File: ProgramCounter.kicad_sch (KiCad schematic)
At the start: 11 parts, among them U601 74LS161, U602 74LS161, U603 74HC245, U604 74HC245, U605 74HC245

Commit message: Working
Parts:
- removed C605, C606: C, symbol Device:C
- removed U605: 74HC245, symbol 74xx:74HC245
- added C805: C, symbol Device:C
- added U805: 74LS32, symbol 74xx:74LS32
- renumbered C601 to C801, C602 to C802, C603 to C803, C604 to C804, U603 to U801, U604 to U802, U601 to U803, U602 to U804
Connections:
- net Bus_{0} is gone; now on net PC_{0}: U801.2 (A0), U802.2 (A0), U803.14 (Q0)
- net Bus_{1} is gone; now on net PC_{1}: U801.3 (A1), U802.3 (A1), U803.13 (Q1)
- net Bus_{2} is gone; now on net PC_{2}: U801.4 (A2), U802.4 (A2), U803.12 (Q2)
- net Bus_{3} is gone; now on net PC_{3}: U801.5 (A3), U802.5 (A3), U803.11 (Q3)
- net Bus_{4} is gone; now on net PC_{4}: U801.6 (A4), U802.6 (A4), U804.14 (Q0)
- net Bus_{5} is gone; now on net PC_{5}: U801.7 (A5), U802.7 (A5), U804.13 (Q1)
- net Bus_{6} is gone; now on net PC_{6}: U801.8 (A6), U802.8 (A6), U804.12 (Q2)
- net Bus_{7} is gone; now on net PC_{7}: U801.9 (A7), U802.9 (A7), U804.11 (Q3)
- net +5V: now also C805.1, U805.14 (VCC)
- net GND: now also C805.2, U805.10, U805.12, U805.13, U805.7 (GND), U805.9
- net ~{LoadHigh}: now also U805.4; no longer U804.9 (~{PE})
- net ~{LoadLow}: now also U805.1; no longer U803.9 (~{PE})
- new net ~{Load}: U805.2, U805.5
- new net ~{PE_High}: U804.9 (~{PE}), U805.6
- new net ~{PE_Low}: U803.9 (~{PE}), U805.3
- no-connect marks 1 -> 3
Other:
- moved on the sheet: C801, C802, C803, C804

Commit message: Reorganize Registerfile
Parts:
- removed C805: C, symbol Device:C
- removed U805: 74LS32, symbol 74xx:74LS32
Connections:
- net ~{PE_High} is gone; now on net ~{LoadHigh}: U804.9 (~{PE})
- net ~{PE_Low} is gone; now on net ~{LoadLow}: U803.9 (~{PE})
- no-connect marks 3 -> 1
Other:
- moved on the sheet: C801, C802, C803, C804

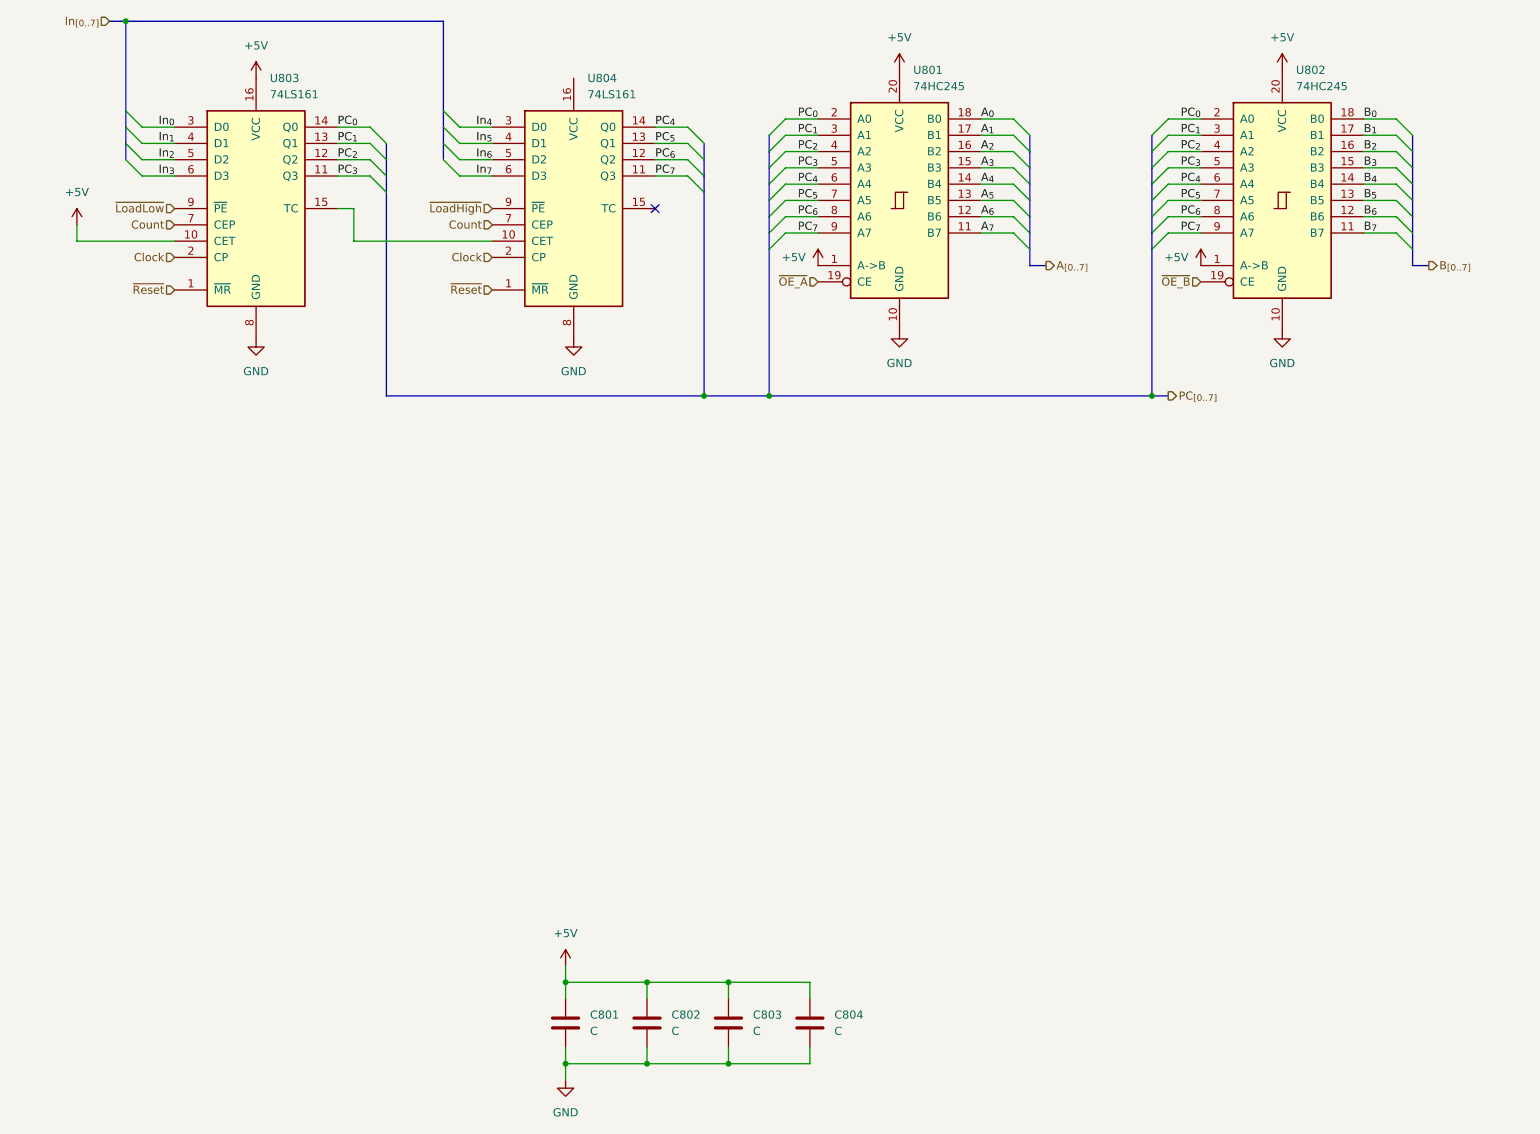
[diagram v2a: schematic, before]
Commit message: More cleanup and preparing signals for control logic
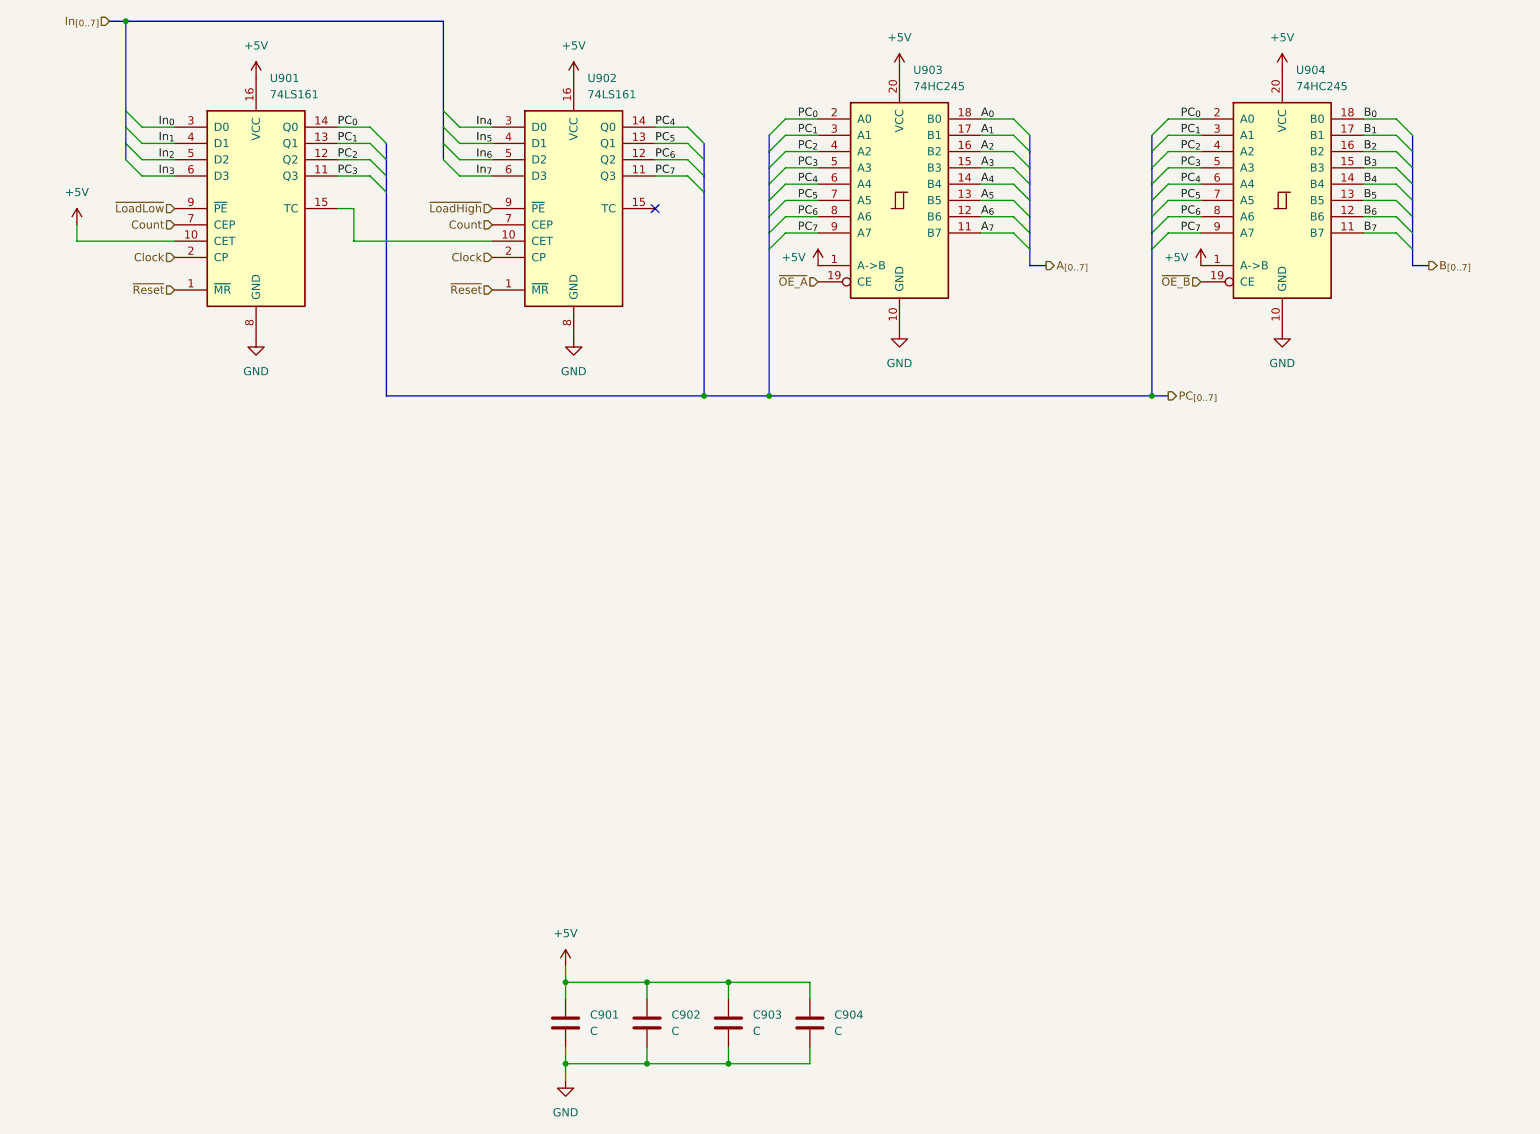
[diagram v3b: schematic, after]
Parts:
- renumbered C801 to C901, C802 to C902, C803 to C903, C804 to C904, U803 to U901, U804 to U902, U801 to U903, U802 to U904
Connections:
- net +5V: now also U902.16 (VCC)
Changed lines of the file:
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@@
 		(dnp no)
 		(fields_autoplaced yes)
-		(property "Reference" "#PWR0804"
+		(property "Reference" "#PWR0901"
 			(at 33.02 62.23 0)
 			(effects
@@
 			(project "BRISC8"
 				(path "/e198223b-f7bd-4b26-ae2e-259db8d07fb6/d081cdcb-1181-4657-9580-dc3ba9a85775/ded358fb-ee52-4096-a32a-0cce52708100/0c7a1bf0-e6ae-42c1-a12c-9c71b98ed1be"
-					(reference "#PWR0804")
+					(reference "#PWR0901")
 					(unit 1)
 				)
@@
 		(on_board yes)
 		(dnp no)
-		(property "Reference" "#PWR0806"
+		(property "Reference" "#PWR0911"
 			(at 208.28 68.58 0)
 			(effects
@@
 			(project "BRISC8"
 				(path "/e198223b-f7bd-4b26-ae2e-259db8d07fb6/d081cdcb-1181-4657-9580-dc3ba9a85775/ded358fb-ee52-4096-a32a-0cce52708100/0c7a1bf0-e6ae-42c1-a12c-9c71b98ed1be"
-					(reference "#PWR0806")
+					(reference "#PWR0911")
 					(unit 1)
 				)
@@
 		(dnp no)
 		(fields_autoplaced yes)
-		(property "Reference" "#PWR0807"
+		(property "Reference" "#PWR0910"
 			(at 161.29 81.28 0)
 			(effects
@@
 			(project "BRISC8"
 				(path "/e198223b-f7bd-4b26-ae2e-259db8d07fb6/d081cdcb-1181-4657-9580-dc3ba9a85775/ded358fb-ee52-4096-a32a-0cce52708100/0c7a1bf0-e6ae-42c1-a12c-9c71b98ed1be"
-					(reference "#PWR0807")
+					(reference "#PWR0910")
 					(unit 1)
 				)
@@
 		(dnp no)
 		(fields_autoplaced yes)
-		(property "Reference" "C801"
+		(property "Reference" "C901"
 			(at 113.03 181.6099 0)
 			(effects
@@
 			(project "BRISC8"
 				(path "/e198223b-f7bd-4b26-ae2e-259db8d07fb6/d081cdcb-1181-4657-9580-dc3ba9a85775/ded358fb-ee52-4096-a32a-0cce52708100/0c7a1bf0-e6ae-42c1-a12c-9c71b98ed1be"
-					(reference "C801")
+					(reference "C901")
 					(unit 1)
 				)
@@
 		(dnp no)
 		(fields_autoplaced yes)
-		(property "Reference" "#PWR0809"
+		(property "Reference" "#PWR0903"
 			(at 60.96 82.55 0)
 			(effects
@@
 			(project "BRISC8"
 				(path "/e198223b-f7bd-4b26-ae2e-259db8d07fb6/d081cdcb-1181-4657-9580-dc3ba9a85775/ded358fb-ee52-4096-a32a-0cce52708100/0c7a1bf0-e6ae-42c1-a12c-9c71b98ed1be"
-					(reference "#PWR0809")
+					(reference "#PWR0903")
 					(unit 1)
 				)
@@
 		(dnp no)
 		(fields_autoplaced yes)
-		(property "Reference" "#PWR0810"
+		(property "Reference" "#PWR0907"
 			(at 110.49 82.55 0)
 			(effects
@@
 			(project "BRISC8"
 				(path "/e198223b-f7bd-4b26-ae2e-259db8d07fb6/d081cdcb-1181-4657-9580-dc3ba9a85775/ded358fb-ee52-4096-a32a-0cce52708100/0c7a1bf0-e6ae-42c1-a12c-9c71b98ed1be"
-					(reference "#PWR0810")
+					(reference "#PWR0907")
 					(unit 1)
 				)
@@
 		(dnp no)
 		(fields_autoplaced yes)
-		(property "Reference" "#PWR0803"
+		(property "Reference" "#PWR0902"
 			(at 60.96 39.37 0)
 			(effects
@@
 			(project "BRISC8"
 				(path "/e198223b-f7bd-4b26-ae2e-259db8d07fb6/d081cdcb-1181-4657-9580-dc3ba9a85775/ded358fb-ee52-4096-a32a-0cce52708100/0c7a1bf0-e6ae-42c1-a12c-9c71b98ed1be"
-					(reference "#PWR0803")
+					(reference "#PWR0902")
 					(unit 1)
 				)
@@
 		(dnp no)
 		(fields_autoplaced yes)
-		(property "Reference" "C802"
+		(property "Reference" "C902"
 			(at 125.73 181.6099 0)
 			(effects
@@
 			(project "BRISC8"
 				(path "/e198223b-f7bd-4b26-ae2e-259db8d07fb6/d081cdcb-1181-4657-9580-dc3ba9a85775/ded358fb-ee52-4096-a32a-0cce52708100/0c7a1bf0-e6ae-42c1-a12c-9c71b98ed1be"
-					(reference "C802")
+					(reference "C902")
 					(unit 1)
 				)
@@
 		(dnp no)
 		(fields_autoplaced yes)
-		(property "Reference" "#PWR0801"
+		(property "Reference" "#PWR0909"
 			(at 161.29 38.1 0)
 			(effects
@@
 			(project "BRISC8"
 				(path "/e198223b-f7bd-4b26-ae2e-259db8d07fb6/d081cdcb-1181-4657-9580-dc3ba9a85775/ded358fb-ee52-4096-a32a-0cce52708100/0c7a1bf0-e6ae-42c1-a12c-9c71b98ed1be"
-					(reference "#PWR0801")
+					(reference "#PWR0909")
 					(unit 1)
 				)
@@
 		(dnp no)
 		(fields_autoplaced yes)
-		(property "Reference" "U801"
+		(property "Reference" "U903"
 			(at 163.4333 34.29 0)
 			(effects
@@
 			(project "BRISC8"
 				(path "/e198223b-f7bd-4b26-ae2e-259db8d07fb6/d081cdcb-1181-4657-9580-dc3ba9a85775/ded358fb-ee52-4096-a32a-0cce52708100/0c7a1bf0-e6ae-42c1-a12c-9c71b98ed1be"
-					(reference "U801")
+					(reference "U903")
 					(unit 1)
 				)
@@
 		(dnp no)
 		(fields_autoplaced yes)
-		(property "Reference" "U803"
+		(property "Reference" "U901"
 			(at 63.1033 35.56 0)
 			(effects
@@
 			(project "BRISC8"
 				(path "/e198223b-f7bd-4b26-ae2e-259db8d07fb6/d081cdcb-1181-4657-9580-dc3ba9a85775/ded358fb-ee52-4096-a32a-0cce52708100/0c7a1bf0-e6ae-42c1-a12c-9c71b98ed1be"
-					(reference "U803")
+					(reference "U901")
 					(unit 1)
 				)
@@
 		(dnp no)
 		(fields_autoplaced yes)
-		(property "Reference" "U804"
+		(property "Reference" "U902"
 			(at 112.6333 35.56 0)
 			(effects
@@
 			(project "BRISC8"
 				(path "/e198223b-f7bd-4b26-ae2e-259db8d07fb6/d081cdcb-1181-4657-9580-dc3ba9a85775/ded358fb-ee52-4096-a32a-0cce52708100/0c7a1bf0-e6ae-42c1-a12c-9c71b98ed1be"
-					(reference "U804")
+					(reference "U902")
 					(unit 1)
 				)
@@
 		(dnp no)
 		(fields_autoplaced yes)
-		(property "Reference" "C804"
+		(property "Reference" "C904"
 			(at 151.13 181.6099 0)
 			(effects
@@
 			(project "BRISC8"
 				(path "/e198223b-f7bd-4b26-ae2e-259db8d07fb6/d081cdcb-1181-4657-9580-dc3ba9a85775/ded358fb-ee52-4096-a32a-0cce52708100/0c7a1bf0-e6ae-42c1-a12c-9c71b98ed1be"
-					(reference "C804")
+					(reference "C904")
 					(unit 1)
 				)
@@
 		(dnp no)
 		(fields_autoplaced yes)
-		(property "Reference" "#PWR0811"
+		(property "Reference" "#PWR0904"
 			(at 109.22 177.8 0)
 			(effects
@@
 			(project "BRISC8"
 				(path "/e198223b-f7bd-4b26-ae2e-259db8d07fb6/d081cdcb-1181-4657-9580-dc3ba9a85775/ded358fb-ee52-4096-a32a-0cce52708100/0c7a1bf0-e6ae-42c1-a12c-9c71b98ed1be"
-					(reference "#PWR0811")
+					(reference "#PWR0904")
 					(unit 1)
 				)
@@
 		(dnp no)
 		(fields_autoplaced yes)
-		(property "Reference" "#PWR0808"
+		(property "Reference" "#PWR0913"
 			(at 220.98 81.28 0)
 			(effects
@@
 			(project "BRISC8"
 				(path "/e198223b-f7bd-4b26-ae2e-259db8d07fb6/d081cdcb-1181-4657-9580-dc3ba9a85775/ded358fb-ee52-4096-a32a-0cce52708100/0c7a1bf0-e6ae-42c1-a12c-9c71b98ed1be"
-					(reference "#PWR0808")
+					(reference "#PWR0913")
 					(unit 1)
 				)
@@
 		(dnp no)
 		(fields_autoplaced yes)
-		(property "Reference" "#PWR0802"
+		(property "Reference" "#PWR0912"
 			(at 220.98 38.1 0)
 			(effects
@@
 			(project "BRISC8"
 				(path "/e198223b-f7bd-4b26-ae2e-259db8d07fb6/d081cdcb-1181-4657-9580-dc3ba9a85775/ded358fb-ee52-4096-a32a-0cce52708100/0c7a1bf0-e6ae-42c1-a12c-9c71b98ed1be"
-					(reference "#PWR0802")
+					(reference "#PWR0912")
 					(unit 1)
 				)
@@
 		(dnp no)
 		(fields_autoplaced yes)
-		(property "Reference" "U802"
+		(property "Reference" "U904"
 			(at 223.1233 34.29 0)
 			(effects
@@
 			(project "BRISC8"
 				(path "/e198223b-f7bd-4b26-ae2e-259db8d07fb6/d081cdcb-1181-4657-9580-dc3ba9a85775/ded358fb-ee52-4096-a32a-0cce52708100/0c7a1bf0-e6ae-42c1-a12c-9c71b98ed1be"
-					(reference "U802")
+					(reference "U904")
 					(unit 1)
 				)
@@
 		(dnp no)
 		(fields_autoplaced yes)
-		(property "Reference" "C803"
+		(property "Reference" "C903"
 			(at 138.43 181.6099 0)
 			(effects
@@
 			(project "BRISC8"
 				(path "/e198223b-f7bd-4b26-ae2e-259db8d07fb6/d081cdcb-1181-4657-9580-dc3ba9a85775/ded358fb-ee52-4096-a32a-0cce52708100/0c7a1bf0-e6ae-42c1-a12c-9c71b98ed1be"
-					(reference "C803")
+					(reference "C903")
+					(unit 1)
+				)
+			)
+		)
+	)
+	(symbol
+		(lib_id "power:+5V")
+		(at 110.49 35.56 0)
+		(unit 1)
+		(exclude_from_sim no)
+		(in_bom yes)
+		(on_board yes)
+		(dnp no)
+		(fields_autoplaced yes)
+		(property "Reference" "#PWR0906"
+			(at 110.49 39.37 0)
+			(effects
+				(font
+					(size 1.27 1.27)
+				)
+				(hide yes)
+			)
+		)
+		(property "Value" "+5V"
+			(at 110.49 30.48 0)
+			(effects
+				(font
+					(size 1.27 1.27)
+				)
+			)
+		)
+		(property "Footprint" ""
+			(at 110.49 35.56 0)
+			(effects
+				(font
+					(size 1.27 1.27)
+				)
+				(hide yes)
+			)
+		)
+		(property "Datasheet" ""
+			(at 110.49 35.56 0)
+			(effects
+				(font
+					(size 1.27 1.27)
+				)
+				(hide yes)
+			)
+		)
+		(property "Description" "Power symbol creates a global label with name \"+5V\""
+			(at 110.49 35.56 0)
+			(effects
+				(font
+					(size 1.27 1.27)
+				)
+				(hide yes)
+			)
+		)
+		(pin "1"
+		)
+		(instances
+			(project "BRISC8"
+				(path "/e198223b-f7bd-4b26-ae2e-259db8d07fb6/d081cdcb-1181-4657-9580-dc3ba9a85775/ded358fb-ee52-4096-a32a-0cce52708100/0c7a1bf0-e6ae-42c1-a12c-9c71b98ed1be"
+					(reference "#PWR0906")
 					(unit 1)
 				)
@@
 		(on_board yes)
 		(dnp no)
-		(property "Reference" "#PWR0805"
+		(property "Reference" "#PWR0908"
 			(at 148.59 68.58 0)
 			(effects
@@
 			(project "BRISC8"
 				(path "/e198223b-f7bd-4b26-ae2e-259db8d07fb6/d081cdcb-1181-4657-9580-dc3ba9a85775/ded358fb-ee52-4096-a32a-0cce52708100/0c7a1bf0-e6ae-42c1-a12c-9c71b98ed1be"
-					(reference "#PWR0805")
+					(reference "#PWR0908")
 					(unit 1)
 				)
@@
 		(dnp no)
 		(fields_autoplaced yes)
-		(property "Reference" "#PWR0812"
+		(property "Reference" "#PWR0905"
 			(at 109.22 198.12 0)
 			(effects
@@
 			(project "BRISC8"
 				(path "/e198223b-f7bd-4b26-ae2e-259db8d07fb6/d081cdcb-1181-4657-9580-dc3ba9a85775/ded358fb-ee52-4096-a32a-0cce52708100/0c7a1bf0-e6ae-42c1-a12c-9c71b98ed1be"
-					(reference "#PWR0812")
-					(unit 1)
-				)
+					(reference "#PWR0905")
+					(unit 1)
+				)
